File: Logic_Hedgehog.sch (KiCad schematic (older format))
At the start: 62 parts, among them J40 RaspberryPI3, J41 UART_EXT_1, J410 Digital, J411 Analog, J412 SERVO, J413 MOTORS, J414 MOTORS, J42 I2C_EXT_0, J43 I2C_EXT_1, J44 SPI_EXT_0_0, J45 SPI_EXT_0_1, J46 SPI_EXT_1, J47 Digital, J48 Analog, J49 SERVO, U40 STM32F401VBT6, U41 IMU_ICM-20689, U42 DRV8835, U43 DRV8835, U44 Buzzer

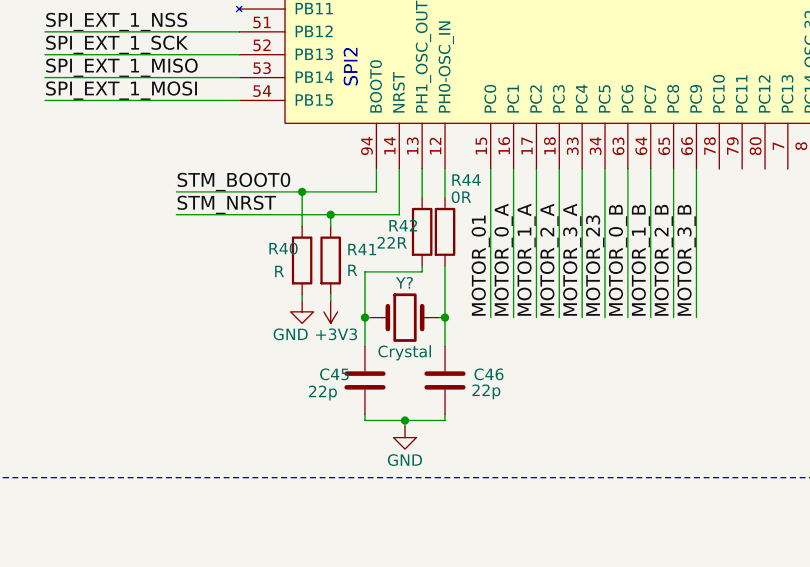
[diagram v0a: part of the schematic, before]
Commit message: linked some footprints
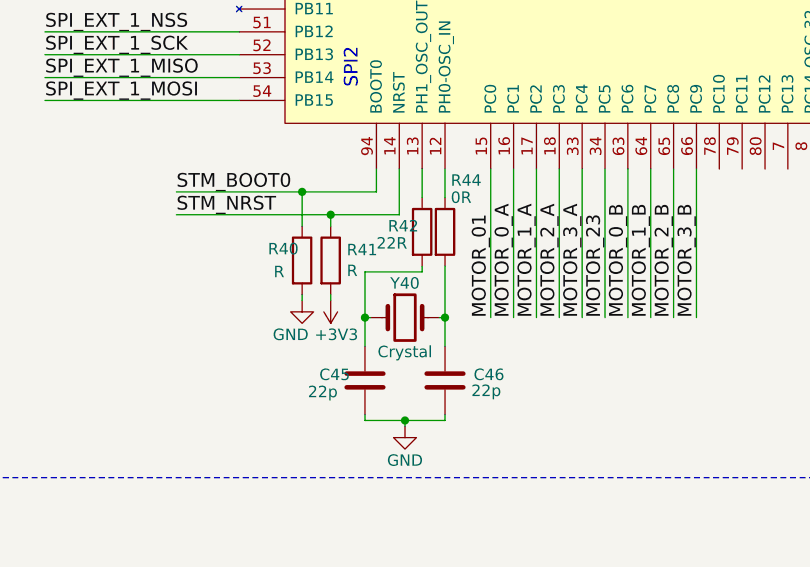
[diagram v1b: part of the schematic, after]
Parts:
- gave numbers to parts that had none: 1

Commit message: added reset and power control stuff, changed some ref.des.
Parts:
- added J43: I2C_EXT_0_EXP, symbol CONN_01X04
- added U41: 74LVC2G32, symbol 74LVC2G32
- added U42: MC74VHC1G126, symbol MC74VHC1G126
- J40: footprint (none) -> Socket_Strips:Socket_Strip_Straight_2x20_Pitch2.54mm
- J41, J42: footprint (none) -> Socket_Strips:Socket_Strip_Straight_1x04_Pitch2.54mm
- J44: renamed from J43; footprint (none) -> Socket_Strips:Socket_Strip_Straight_1x04_Pitch2.54mm
- J45: renamed from J44; footprint (none) -> Socket_Strips:Socket_Strip_Straight_1x06_Pitch2.54mm
- J46: renamed from J45; footprint (none) -> Socket_Strips:Socket_Strip_Straight_1x06_Pitch2.54mm
- J47: renamed from J46; footprint (none) -> Socket_Strips:Socket_Strip_Straight_1x06_Pitch2.54mm
- J48: renamed from J47; footprint (none) -> Socket_Strips:Socket_Strip_Straight_1x08_Pitch2.54mm
- J49: renamed from J48; footprint (none) -> Socket_Strips:Socket_Strip_Straight_1x08_Pitch2.54mm
- J50: renamed from J410; footprint (none) -> Socket_Strips:Socket_Strip_Straight_2x08_Pitch2.54mm
- J51: renamed from J411; footprint (none) -> Socket_Strips:Socket_Strip_Straight_2x08_Pitch2.54mm
- J52: renamed from J49; footprint (none) -> Pin_Headers:Pin_Header_Straight_1x04_Pitch2.54mm
- J53: renamed from J412; footprint (none) -> Pin_Headers:Pin_Header_Straight_2x04_Pitch2.54mm
- J54: renamed from J413; footprint (none) -> Socket_Strips:Socket_Strip_Angled_1x04_Pitch2.54mm
- J55: renamed from J414; footprint (none) -> Socket_Strips:Socket_Strip_Angled_1x04_Pitch2.54mm
- U40: footprint (none) -> hedgehog_footprints:LQFP_100
- renumbered C410 to C50, C411 to C51, C412 to C52, C414 to C53, C413 to C54, C415 to C55, C416 to C56, C417 to C57, C418 to C58, D410 to D50, R410 to R50, U41 to U43, U42 to U44, U43 to U45, U44 to U46
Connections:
- net +3V3: now also R41.1, J43.2 (P2), U41.8 (VCC), U42.5 (VCC); no longer R41.2
- net EN_PWR_IN: now also U41.7 (OUT1); no longer U40.57 (PD10)
- net EN_Reg_RPi: now also U41.3 (OUT2); no longer U40.55 (PD8)
- net GND: now also U40.37 (PB2), J43.1 (P1), U41.4 (GND), U42.3 (GND)
- net I2C_EXT_0_SCL: now also J43.3 (P3)
- net I2C_EXT_0_SDA: now also J43.4 (P4)
- net STM_NRST: now also R41.2, U42.4 (OUT); no longer J40.29 (GPIO05), R41.1
- net EN_PWR_IN_RPi: now reaches J40.16 (GPIO23)
- net EN_PWR_IN_RPi: now also U41.2 (IN1B)
- net RPi_ACTIVE: now reaches J40.17 (3V3)
- net RPi_ACTIVE: now also U40.78 (PC10)
- net EN_Reg_RPi_RPi: now reaches J40.18 (GPIO24)
- net EN_Reg_RPi_RPi: now also U41.6 (IN2B)
- net STM_NRST_EN_RPi: now reaches J40.37 (GPIO26)
- net STM_NRST_EN_RPi: now also U42.1 (OE)
- new net EN_PWR_IN_STM: U40.57 (PD10), U41.1 (IN1A)
- new net EN_Reg_RPi_STM: U40.55 (PD8), U41.5 (IN2A)
- new net STM_NRST_RPi: J40.29 (GPIO05), U42.2 (IN)
- no-connect marks 12 -> 19
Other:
- note added: "2x OR-Gate"
- note added: "Power- and STM-Reset-Control"
- note removed: "pi resets stm during boot/when off?\nhigh on reset line when pi off -> bad for pi?"
- moved on the sheet: C41, C42, C43, C44, C45, C46, C47, C48, C49, C50, C51, J40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

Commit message: added footprint for Buzzer, Pushbutton and HSOP-8
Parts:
- U41: footprint (none) -> Housings_SSOP:VSSOP-8_2.3x2mm_Pitch0.5mm
- U42: footprint (none) -> TO_SOT_Packages_SMD:SOT-23-5
- U43: footprint (none) -> hedgehog_footprints:QFN-24_3x3mm
- U46: footprint (none) -> hedgehog_footprints:Buzzer
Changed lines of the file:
@@
 LIBS:switches
 LIBS:Hedgehog-cache
-EELAYER 26 0
+EELAYER 25 0
 EELAYER END
 $Descr A3 16535 11693
@@
 F 0 "U46" H 14375 9450 60  0000 C CNN
 F 1 "Buzzer" H 14450 9375 60  0000 C CNN
-F 2 "" H 14175 9400 60  0001 C CNN
+F 2 "hedgehog_footprints:Buzzer" H 14175 9400 60  0001 C CNN
 F 3 "" H 14175 9400 60  0001 C CNN
 	1    14175 9400
@@
 F 0 "U43" H 9575 10600 60  0000 L CNN
 F 1 "IMU_ICM-20689" H 9100 9675 60  0000 L CNN
-F 2 "" H 10250 9700 60  0001 C CNN
+F 2 "hedgehog_footprints:QFN-24_3x3mm" H 10250 9700 60  0001 C CNN
 F 3 "" H 10250 9700 60  0001 C CNN
 	1    10100 10200
@@
 F 0 "U42" H 6700 10450 60  0000 C CNN
 F 1 "MC74VHC1G126" H 6700 9850 60  0000 C CNN
-F 2 "" H 6700 10150 60  0001 C CNN
+F 2 "TO_SOT_Packages_SMD:SOT-23-5" H 6700 10150 60  0001 C CNN
 F 3 "" H 6700 10150 60  0001 C CNN
 	1    6700 10150
@@
 F 0 "U41" H 6700 9550 60  0000 C CNN
 F 1 "74LVC2G32" H 6700 8800 60  0000 C CNN
-F 2 "" H 6700 9000 60  0001 C CNN
+F 2 "Housings_SSOP:VSSOP-8_2.3x2mm_Pitch0.5mm" H 6700 9000 60  0001 C CNN
 F 3 "" H 6700 9000 60  0001 C CNN
 	1    6700 9000

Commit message: added HSOP-8,LSON-22,Mini-F3-B,MSOP-10,SOD323F Footprint finished package assignment (without inductors )
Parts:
- C40, C45, C46, C47, C48, C50, C51, C52, C54, C56, C57, C58: footprint (none) -> Capacitors_SMD:C_0603_HandSoldering
- C41, C42, C43, C44: footprint (none) -> Capacitors_SMD:C_0402
- C49, C53, C55: footprint (none) -> Capacitors_SMD:C_0805_HandSoldering
- D40, D41, D42, D43: footprint (none) -> LEDs:LED_0805
- D44, D45, D46, D47, D48, D49, D50: footprint (none) -> hedgehog_footprints:SOD323F
- L40: footprint (none) -> Inductors_SMD:L_0603_HandSoldering
- R40, R41, R42, R45, R46, R47, R48, R49, R50: footprint (none) -> Resistors_SMD:R_0603_HandSoldering
- R44: footprint (none) -> Resistors_SMD:R_0402
- Y40: footprint (none) -> Crystals:Crystal_HC49-U_Vertical
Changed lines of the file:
@@
 F 0 "R48" V 11575 1575 50  0000 C CNN
 F 1 "330R" V 11575 1800 50  0000 C CNN
-F 2 "" V 11580 1725 50  0001 C CNN
+F 2 "Resistors_SMD:R_0603_HandSoldering" V 11580 1725 50  0001 C CNN
 F 3 "" H 11650 1725 50  0001 C CNN
 	1    11650 1725
@@
 F 0 "R47" V 11575 1375 50  0000 C CNN
 F 1 "330R" V 11575 1600 50  0000 C CNN
-F 2 "" V 11580 1525 50  0001 C CNN
+F 2 "Resistors_SMD:R_0603_HandSoldering" V 11580 1525 50  0001 C CNN
 F 3 "" H 11650 1525 50  0001 C CNN
 	1    11650 1525
@@
 F 0 "D41" H 11200 1825 50  0000 C CNN
 F 1 "LED" H 11350 1675 50  0000 C CNN
-F 2 "" H 11200 1725 50  0001 C CNN
+F 2 "LEDs:LED_0805" H 11200 1725 50  0001 C CNN
 F 3 "" H 11200 1725 50  0001 C CNN
 	1    11200 1725
@@
 F 0 "D40" H 11200 1625 50  0000 C CNN
 F 1 "LED" H 11350 1475 50  0000 C CNN
-F 2 "" H 11200 1525 50  0001 C CNN
+F 2 "LEDs:LED_0805" H 11200 1525 50  0001 C CNN
 F 3 "" H 11200 1525 50  0001 C CNN
 	1    11200 1525
@@
 F 0 "C56" V 14700 2575 50  0000 C CNN
 F 1 "1µ" V 14800 2575 50  0000 C CNN
-F 2 "" H 14788 2300 50  0001 C CNN
+F 2 "Capacitors_SMD:C_0603_HandSoldering" H 14788 2300 50  0001 C CNN
 F 3 "" H 14750 2450 50  0001 C CNN
 	1    14750 2450
@@
 F 0 "C57" V 14700 4325 50  0000 C CNN
 F 1 "1µ" V 14800 4325 50  0000 C CNN
-F 2 "" H 14788 4050 50  0001 C CNN
+F 2 "Capacitors_SMD:C_0603_HandSoldering" H 14788 4050 50  0001 C CNN
 F 3 "" H 14750 4200 50  0001 C CNN
 	1    14750 4200
@@
 F 0 "C58" V 14700 5650 50  0000 C CNN
 F 1 "1µ" V 14800 5650 50  0000 C CNN
-F 2 "" H 14788 5375 50  0001 C CNN
+F 2 "Capacitors_SMD:C_0603_HandSoldering" H 14788 5375 50  0001 C CNN
 F 3 "" H 14750 5525 50  0001 C CNN
 	1    14750 5525
@@
 F 0 "R41" H 7400 9925 50  0000 L CNN
 F 1 "R" H 7400 9850 50  0000 L CNN
-F 2 "" V 7280 9900 50  0001 C CNN
+F 2 "Resistors_SMD:R_0603_HandSoldering" V 7280 9900 50  0001 C CNN
 F 3 "" H 7350 9900 50  0001 C CNN
 	1    7350 9900
@@
 F 0 "R40" H 3800 6575 50  0000 L CNN
 F 1 "R" H 3800 6475 50  0000 L CNN
-F 2 "" V 3930 6525 50  0001 C CNN
+F 2 "Resistors_SMD:R_0603_HandSoldering" V 3930 6525 50  0001 C CNN
 F 3 "" H 4000 6525 50  0001 C CNN
 	1    4000 6525
@@
 F 0 "R42" H 4325 6425 50  0000 L CNN
 F 1 "22R" H 4325 6350 50  0000 L CNN
-F 2 "" V 4455 6400 50  0001 C CNN
+F 2 "Resistors_SMD:R_0603_HandSoldering" V 4455 6400 50  0001 C CNN
 F 3 "" H 4525 6400 50  0001 C CNN
 	1    4525 6400
@@
 F 0 "R44" H 4650 6625 50  0000 L CNN
 F 1 "0R" H 4650 6550 50  0000 L CNN
-F 2 "" V 4555 6400 50  0001 C CNN
+F 2 "Resistors_SMD:R_0402" V 4555 6400 50  0001 C CNN
 F 3 "" H 4625 6400 50  0001 C CNN
 	1    4625 6400
@@
 F 0 "Y40" H 4450 6925 50  0000 C CNN
 F 1 "Crystal" H 4450 6625 50  0000 C CNN
-F 2 "" H 4450 6775 50  0001 C CNN
+F 2 "Crystals:Crystal_HC49-U_Vertical" H 4450 6775 50  0001 C CNN
 F 3 "" H 4450 6775 50  0001 C CNN
 	1    4450 6775
@@
 F 0 "C45" H 4025 7075 50  0000 L CNN
 F 1 "22p" H 4025 7000 50  0000 L CNN
-F 2 "" H 4313 6900 50  0001 C CNN
+F 2 "Capacitors_SMD:C_0603_HandSoldering" H 4313 6900 50  0001 C CNN
 F 3 "" H 4275 7050 50  0001 C CNN
 	1    4275 7050
@@
 F 0 "C46" H 4725 7075 50  0000 L CNN
 F 1 "22p" H 4725 7000 50  0000 L CNN
-F 2 "" H 4663 6900 50  0001 C CNN
+F 2 "Capacitors_SMD:C_0603_HandSoldering" H 4663 6900 50  0001 C CNN
 F 3 "" H 4625 7050 50  0001 C CNN
 	1    4625 7050
@@
 F 0 "C47" V 5550 1925 50  0000 C CNN
 F 1 "2µ2" V 5550 2125 50  0000 C CNN
-F 2 "" H 5738 1875 50  0001 C CNN
+F 2 "Capacitors_SMD:C_0603_HandSoldering" H 5738 1875 50  0001 C CNN
 F 3 "" H 5700 2025 50  0001 C CNN
 	1    5700 2025
@@
 F 0 "C48" V 5650 2100 50  0000 C CNN
 F 1 "2µ2" V 5825 2225 50  0000 C CNN
-F 2 "" H 5738 2075 50  0001 C CNN
+F 2 "Capacitors_SMD:C_0603_HandSoldering" H 5738 2075 50  0001 C CNN
 F 3 "" H 5700 2225 50  0001 C CNN
 	1    5700 2225
@@
 F 0 "C44" V 3925 2500 50  0000 L CNN
 F 1 "100n" V 3850 2500 50  0000 L CNN
-F 2 "" H 3913 2150 50  0001 C CNN
+F 2 "Capacitors_SMD:C_0402" H 3913 2150 50  0001 C CNN
 F 3 "" H 3875 2300 50  0001 C CNN
 	1    3875 2300
@@
 F 0 "C43" V 3900 2275 50  0000 L CNN
 F 1 "100n" V 3825 2275 50  0000 L CNN
-F 2 "" H 3913 1925 50  0001 C CNN
+F 2 "Capacitors_SMD:C_0402" H 3913 1925 50  0001 C CNN
 F 3 "" H 3875 2075 50  0001 C CNN
 	1    3875 2075
@@
 F 0 "C42" V 3900 2050 50  0000 L CNN
 F 1 "100n" V 3825 2050 50  0000 L CNN
-F 2 "" H 3913 1700 50  0001 C CNN
+F 2 "Capacitors_SMD:C_0402" H 3913 1700 50  0001 C CNN
 F 3 "" H 3875 1850 50  0001 C CNN
 	1    3875 1850
@@
 F 0 "C41" V 3900 1825 50  0000 L CNN
 F 1 "100n" V 3825 1800 50  0000 L CNN
-F 2 "" H 3913 1475 50  0001 C CNN
+F 2 "Capacitors_SMD:C_0402" H 3913 1475 50  0001 C CNN
 F 3 "" H 3875 1625 50  0001 C CNN
 	1    3875 1625
@@
 F 0 "C40" H 1975 1700 50  0000 L CNN
 F 1 "1µ" H 2000 1625 50  0000 L CNN
-F 2 "" H 1913 1500 50  0001 C CNN
+F 2 "Capacitors_SMD:C_0603_HandSoldering" H 1913 1500 50  0001 C CNN
 F 3 "" H 1875 1650 50  0001 C CNN
 	1    1875 1650
@@
 F 0 "L40" V 1750 1425 50  0000 C CNN
 F 1 "39n" V 1625 1425 50  0000 C CNN
-F 2 "" H 1675 1425 50  0001 C CNN
+F 2 "Inductors_SMD:L_0603_HandSoldering" H 1675 1425 50  0001 C CNN
 F 3 "" H 1675 1425 50  0001 C CNN
 	1    1675 1425
@@
 F 0 "R50" V 11575 2000 50  0000 C CNN
 F 1 "330R" V 11575 2225 50  0000 C CNN
-F 2 "" V 11580 2150 50  0001 C CNN
+F 2 "Resistors_SMD:R_0603_HandSoldering" V 11580 2150 50  0001 C CNN
 F 3 "" H 11650 2150 50  0001 C CNN
 	1    11650 2150
@@
 F 0 "R49" V 11575 1800 50  0000 C CNN
 F 1 "330R" V 11575 2025 50  0000 C CNN
-F 2 "" V 11580 1950 50  0001 C CNN
+F 2 "Resistors_SMD:R_0603_HandSoldering" V 11580 1950 50  0001 C CNN
 F 3 "" H 11650 1950 50  0001 C CNN
 	1    11650 1950
@@
 F 0 "D43" H 11200 2250 50  0000 C CNN
 F 1 "LED" H 11350 2100 50  0000 C CNN
-F 2 "" H 11200 2150 50  0001 C CNN
+F 2 "LEDs:LED_0805" H 11200 2150 50  0001 C CNN
 F 3 "" H 11200 2150 50  0001 C CNN
 	1    11200 2150
@@
 F 0 "D42" H 11200 2050 50  0000 C CNN
 F 1 "LED" H 11350 1900 50  0000 C CNN
-F 2 "" H 11200 1950 50  0001 C CNN
+F 2 "LEDs:LED_0805" H 11200 1950 50  0001 C CNN
 F 3 "" H 11200 1950 50  0001 C CNN
 	1    11200 1950
@@
 F 0 "C51" H 8900 10400 50  0000 L CNN
 F 1 "0µ47" H 8850 10575 50  0000 L CNN
-F 2 "" H 9113 10325 50  0001 C CNN
+F 2 "Capacitors_SMD:C_0603_HandSoldering" H 9113 10325 50  0001 C CNN
 F 3 "" H 9075 10475 50  0001 C CNN
 	1    9075 10475
@@
 F 0 "C50" H 8975 10200 50  0000 L CNN
 F 1 "2µ2" H 8975 10375 50  0000 L CNN
-F 2 "" H 8988 10125 50  0001 C CNN
+F 2 "Capacitors_SMD:C_0603_HandSoldering" H 8988 10125 50  0001 C CNN
 F 3 "" H 8950 10275 50  0001 C CNN
 	1    8950 10275
@@
 F 0 "C49" H 8800 10200 50  0000 L CNN
 F 1 "100n" H 8750 10375 50  0000 L CNN
-F 2 "" H 8763 10125 50  0001 C CNN
+F 2 "Capacitors_SMD:C_0805_HandSoldering" H 8763 10125 50  0001 C CNN
 F 3 "" H 8725 10275 50  0001 C CNN
 	1    8725 10275
@@
 F 0 "D44" H 11250 7975 50  0000 C CNN
 F 1 "3V6" H 11525 7975 50  0000 C CNN
-F 2 "" H 11400 7925 50  0001 C CNN
+F 2 "hedgehog_footprints:SOD323F" H 11400 7925 50  0001 C CNN
 F 3 "" H 11400 7925 50  0001 C CNN
 	1    11400 7925
@@
 F 0 "D45" H 11250 8100 50  0000 C CNN
 F 1 "3V6" H 11525 8100 50  0000 C CNN
-F 2 "" H 11400 8050 50  0001 C CNN
+F 2 "hedgehog_footprints:SOD323F" H 11400 8050 50  0001 C CNN
 F 3 "" H 11400 8050 50  0001 C CNN
 	1    11400 8050
@@
 F 0 "D46" H 11250 8225 50  0000 C CNN
 F 1 "3V6" H 11525 8225 50  0000 C CNN
-F 2 "" H 11400 8175 50  0001 C CNN
+F 2 "hedgehog_footprints:SOD323F" H 11400 8175 50  0001 C CNN
 F 3 "" H 11400 8175 50  0001 C CNN
 	1    11400 8175
@@
 F 0 "D47" H 11250 8350 50  0000 C CNN
 F 1 "3V6" H 11525 8350 50  0000 C CNN
-F 2 "" H 11400 8300 50  0001 C CNN
+F 2 "hedgehog_footprints:SOD323F" H 11400 8300 50  0001 C CNN
 F 3 "" H 11400 8300 50  0001 C CNN
 	1    11400 8300
@@
 F 0 "D48" H 11250 8475 50  0000 C CNN
 F 1 "3V6" H 11525 8475 50  0000 C CNN
-F 2 "" H 11400 8425 50  0001 C CNN
+F 2 "hedgehog_footprints:SOD323F" H 11400 8425 50  0001 C CNN
 F 3 "" H 11400 8425 50  0001 C CNN
 	1    11400 8425
@@
 F 0 "D49" H 11250 8600 50  0000 C CNN
 F 1 "3V6" H 11525 8600 50  0000 C CNN
-F 2 "" H 11400 8550 50  0001 C CNN
+F 2 "hedgehog_footprints:SOD323F" H 11400 8550 50  0001 C CNN
 F 3 "" H 11400 8550 50  0001 C CNN
 	1    11400 8550
@@
 F 0 "D50" H 11250 8725 50  0000 C CNN
 F 1 "3V6" H 11525 8725 50  0000 C CNN
-F 2 "" H 11400 8675 50  0001 C CNN
+F 2 "hedgehog_footprints:SOD323F" H 11400 8675 50  0001 C CNN
 F 3 "" H 11400 8675 50  0001 C CNN
 	1    11400 8675
@@
 F 0 "R46" H 10175 5125 50  0000 C CNN
 F 1 "1k8" H 10150 5200 50  0000 C CNN
-F 2 "" V 10205 5175 50  0001 C CNN
+F 2 "Resistors_SMD:R_0603_HandSoldering" V 10205 5175 50  0001 C CNN
 F 3 "" H 10275 5175 50  0001 C CNN
 	1    10275 5175
@@
 F 0 "R45" H 10300 5125 50  0000 C CNN
 F 1 "1k8" H 10300 5200 50  0000 C CNN
-F 2 "" V 10105 5175 50  0001 C CNN
+F 2 "Resistors_SMD:R_0603_HandSoldering" V 10105 5175 50  0001 C CNN
 F 3 "" H 10175 5175 50  0001 C CNN
 	1    10175 5175
@@
 F 0 "C53" H 13100 7325 50  0000 L CNN
 F 1 "100n" H 13100 7175 50  0000 L CNN
-F 2 "" H 13113 7100 50  0001 C CNN
+F 2 "Capacitors_SMD:C_0805_HandSoldering" H 13113 7100 50  0001 C CNN
 F 3 "" H 13075 7250 50  0001 C CNN
 	1    13075 7250
@@
 F 0 "C55" H 13100 8450 50  0000 L CNN
 F 1 "100n" H 13100 8300 50  0000 L CNN
-F 2 "" H 13113 8225 50  0001 C CNN
+F 2 "Capacitors_SMD:C_0805_HandSoldering" H 13113 8225 50  0001 C CNN
 F 3 "" H 13075 8375 50  0001 C CNN
 	1    13075 8375
@@
 F 0 "C52" H 12725 7325 50  0000 L CNN
 F 1 "10µ" H 12725 7175 50  0000 L CNN
-F 2 "" H 12738 7100 50  0001 C CNN
+F 2 "Capacitors_SMD:C_0603_HandSoldering" H 12738 7100 50  0001 C CNN
 F 3 "" H 12700 7250 50  0001 C CNN
 	1    12700 7250
@@
 F 0 "C54" H 12725 8450 50  0000 L CNN
 F 1 "10µ" H 12725 8300 50  0000 L CNN
-F 2 "" H 12738 8225 50  0001 C CNN
+F 2 "Capacitors_SMD:C_0603_HandSoldering" H 12738 8225 50  0001 C CNN
 F 3 "" H 12700 8375 50  0001 C CNN
 	1    12700 8375
